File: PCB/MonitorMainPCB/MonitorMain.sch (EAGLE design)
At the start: 1 part, among them U1 ADS1298CZXGT

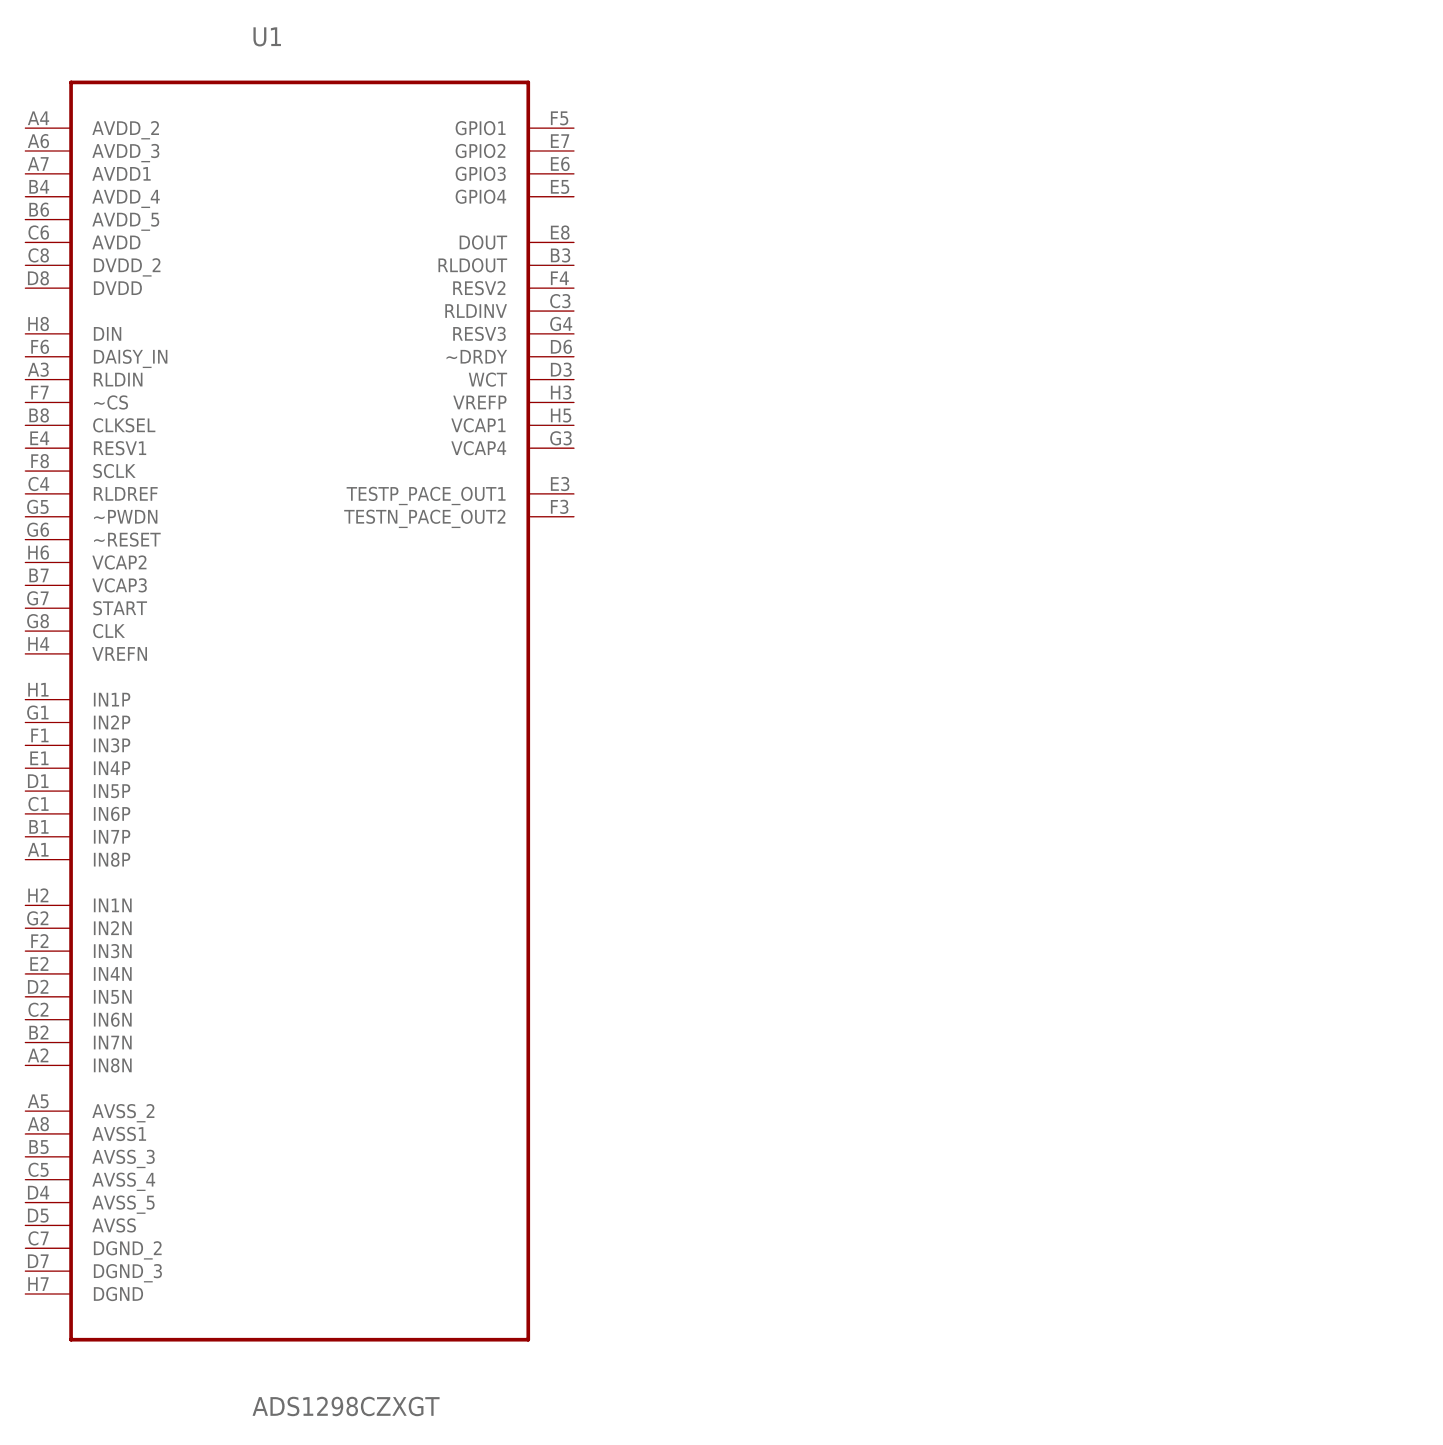
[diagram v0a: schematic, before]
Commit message: Add TI ADS1293 stuff
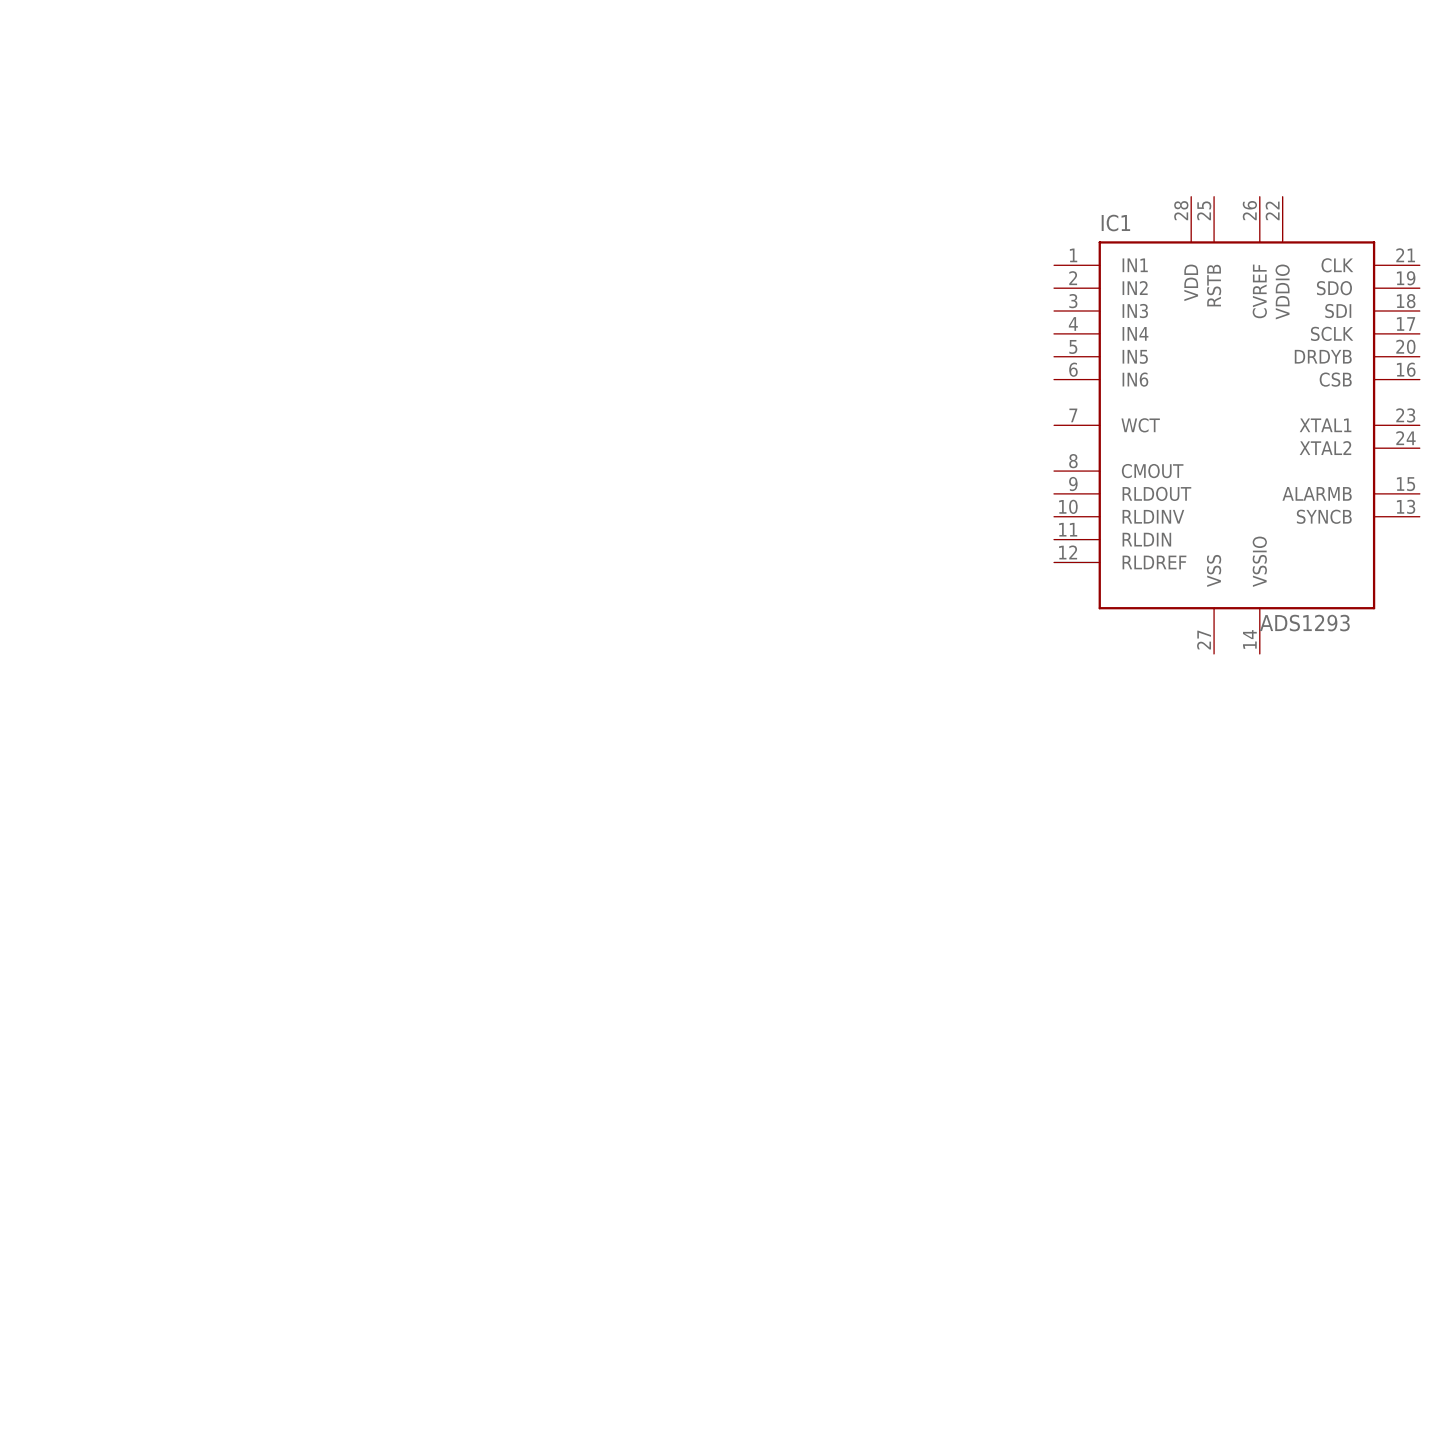
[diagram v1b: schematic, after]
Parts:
- removed U1: ADS1298CZXGT, Texas Instruments_By_element14_Batch_1:ADS1298CZXGT
- added IC1: ADS1293, texas-ads1293:ADS1293
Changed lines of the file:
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@@
 <layer number="51" name="tDocu" color="7" fill="1" visible="no" active="no"/>
 <layer number="52" name="bDocu" color="7" fill="1" visible="no" active="no"/>
+<layer number="53" name="tGND_GNDA" color="7" fill="9" visible="no" active="no"/>
+<layer number="54" name="bGND_GNDA" color="1" fill="9" visible="no" active="no"/>
 <layer number="88" name="SimResults" color="9" fill="1" visible="yes" active="yes"/>
 <layer number="89" name="SimProbes" color="9" fill="1" visible="yes" active="yes"/>
@@
 <layer number="97" name="Info" color="7" fill="1" visible="yes" active="yes"/>
 <layer number="98" name="Guide" color="6" fill="1" visible="yes" active="yes"/>
+<layer number="99" name="SpiceOrder" color="5" fill="1" visible="no" active="no"/>
 </layers>
 <schematic xreflabel="%F%N/%S.%C%R" xrefpart="/%S.%C%R">
@@
 </classes>
 <parts>
-<part name="U1" library="Texas Instruments_By_element14_Batch_1" deviceset="ADS1298CZXGT" device=""/>
+<part name="IC1" library="texas-ads1293" deviceset="ADS1293" device=""/>
 </parts>
 <sheets>
@@
 </plain>
 <instances>
-<instance part="U1" gate="A" x="78.74" y="99.06"/>
+<instance part="IC1" gate="G$1" x="182.88" y="127"/>
 </instances>
 <busses>
